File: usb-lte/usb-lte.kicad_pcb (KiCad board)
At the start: 4 copper layers, 26 x 45 mm, 58 parts, among them J1 Sim slot, J2 Conn_Coaxial, J3 Conn_Coaxial, J4 Conn_Coaxial, J5 Conn_01x02_Pin, P1 USB_C_Plug_USB2.0, Q1 BC847W, Q2 BC847W, U1 AP2112K-3.3, U2 EG95

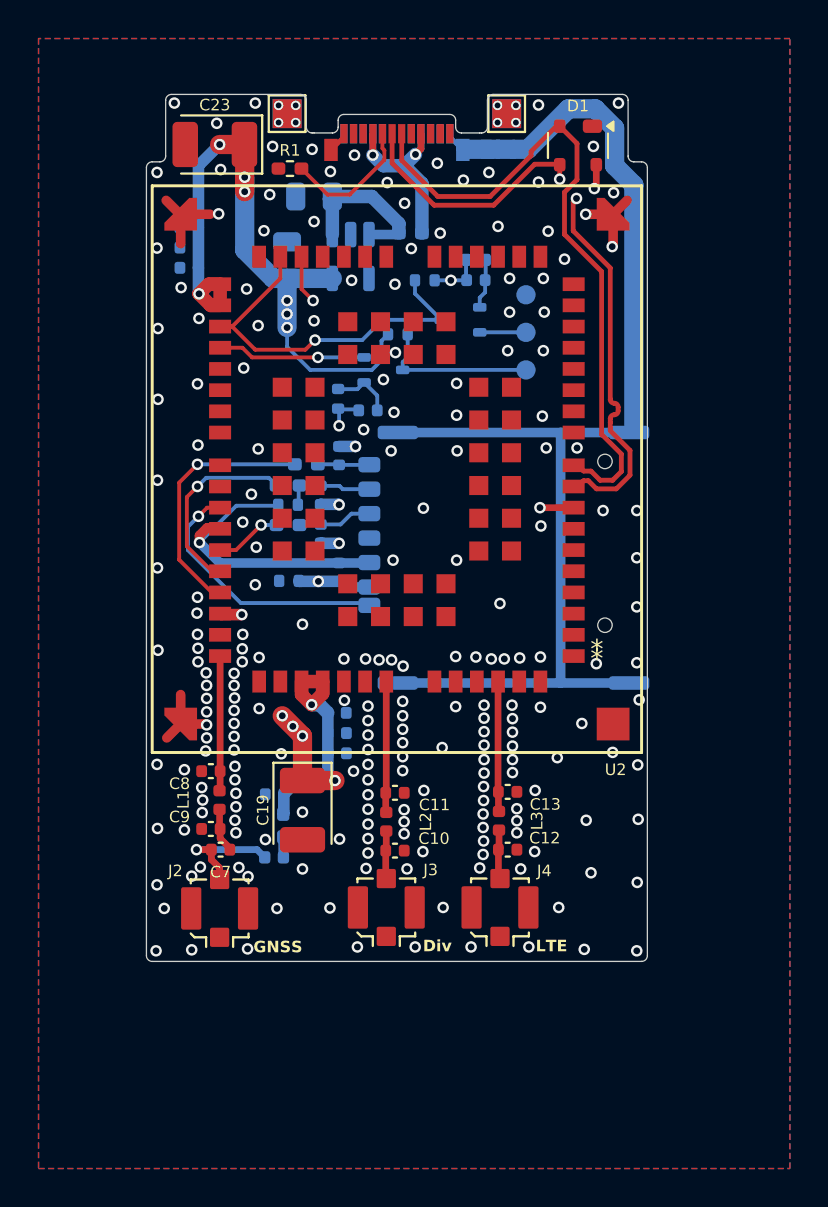
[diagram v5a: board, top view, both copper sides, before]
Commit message: Use SMPS and 3.8V for module
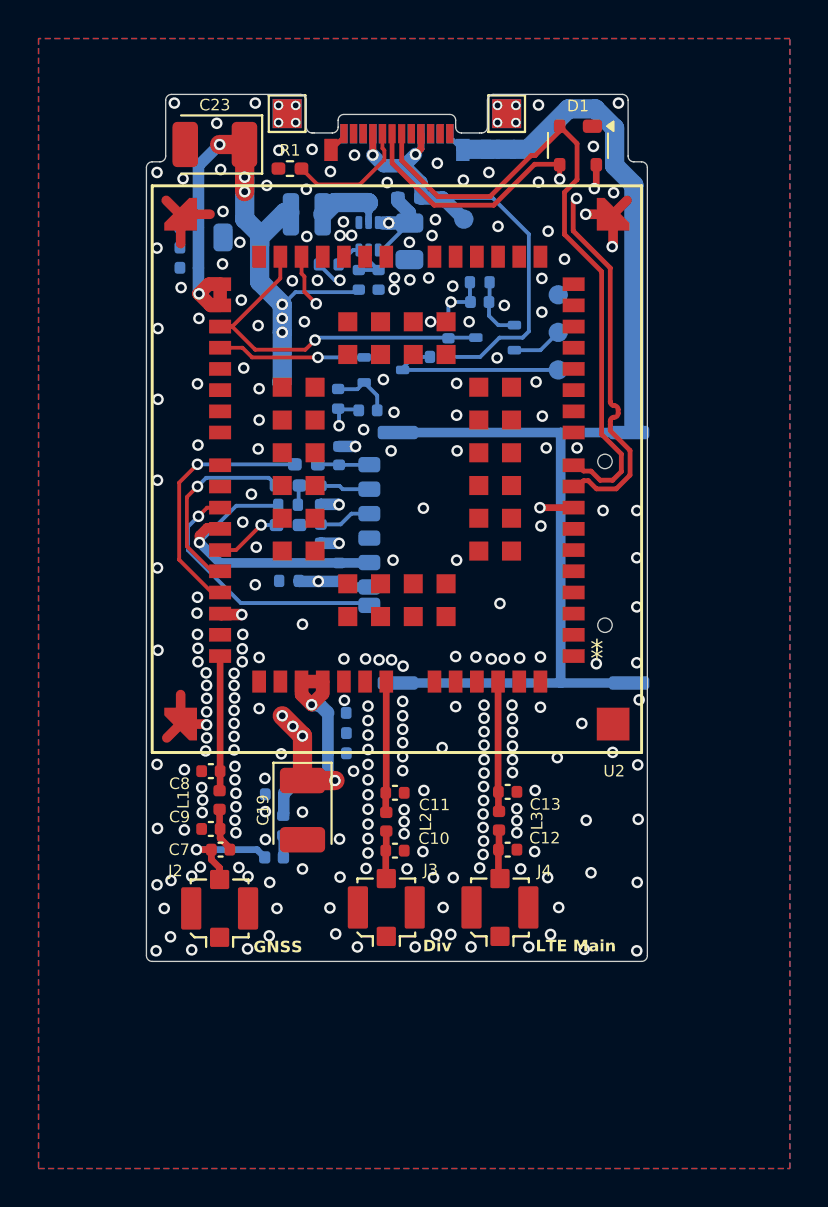
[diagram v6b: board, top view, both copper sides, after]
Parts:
- added L5: 1uH, Inductor_SMD:L_APV_ANR252012, B.Cu at (145.9, 95.1)
- added R13: 510k, Resistor_SMD:R_0402_1005Metric, B.Cu at (148.6, 98.5)
- added R14: 100k, Resistor_SMD:R_0402_1005Metric, B.Cu at (149.7, 98.5)
- added R15: 499k, Resistor_SMD:R_0402_1005Metric, B.Cu at (147.1, 97.7)
- added TP8: TestPoint, footprints:TestPoint_Pad_1mm, B.Cu at (154.1, 95.4)
- added TP9: TestPoint, footprints:TestPoint_Pad_1mm, B.Cu at (144.6, 103.8)
- C1: value 10uF -> 4.7uF
- C2: value 10uF -> 22uF
- R5: footprint Resistor_SMD:R_0402_1005Metric_Pad0.72x0.64mm_HandSolder -> Resistor_SMD:R_0402_1005Metric
- U1: value AP2112K-3.3 -> TPS62A02APDDC; footprint Package_TO_SOT_SMD:SOT-23-5 -> Package_TO_SOT_SMD:SOT-563
- moved C1 5.47 mm to (151.2, 96.5), turned to -90 degrees
- moved R10 2.78 mm to (153.3, 101.0), turned to 90 degrees
- moved C2 2.65 mm to (142.5, 96.3), turned to 0 degrees
- moved R9 2.47 mm to (152.8, 102.5), turned to 180 degrees
- moved Q2 2.02 mm to (155.7, 101.5)
- moved R8 1.83 mm to (151.2, 94.3)
- moved TP5 1.67 mm to (159.0, 103.2)
- moved TP6 1.67 mm to (159.0, 101.2)
- moved TP7 1.67 mm to (159.0, 99.3)
- moved U1 1.40 mm to (149.1, 96.3)
- moved R12 1.18 mm to (154.9, 98.7)
- moved C15 1.15 mm to (154.9, 99.7)
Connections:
- net UART_RX_3V3 renamed UART_RX_5V
- net UART_TX_3V3 renamed UART_TX_5V
- C16 pad 1: +3V3 -> VDD
- C17 pad 1: +3V3 -> VDD
- C18 pad 1: +3V3 -> VDD
- C19 pad 1: +3V3 -> VDD
- C2 pad 1: +3V3 -> GND
- C2 pad 2: GND -> VDD
- C20 pad 1: +3V3 -> VDD
- C21 pad 1: +3V3 -> VDD
- C22 pad 1: +3V3 -> VDD
- C23 pad 1: +3V3 -> VDD
- C24 pad 1: +3V3 -> VDD
- R5 pad 2: +3V3 -> VDD
- R9 pad 1: +3V3 -> VBUS
- U1 pad 1: Net-(U1-EN) -> GND
- U1 pad 2: GND -> Net-(U1-SW)
- U1 pad 4: unconnected-(U1-NC-Pad4) -> Net-(U1-EN)
- U1 pad 5: +3V3 -> Net-(U1-FB)
- U2 pad 32: +3V3 -> VDD
- U2 pad 33: +3V3 -> VDD
- U2 pad 52: +3V3 -> VDD
- U2 pad 53: +3V3 -> VDD
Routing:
- net +3V3: track 76.3 -> 0.00 mm, vias 12 -> 0
- net VDD: track 0.00 -> 73.9 mm, vias 0 -> 12
- net VBUS: track 43.0 -> 58.8 mm
- net Net-(U1-SW): track 0.00 -> 3.66 mm
- net Net-(U1-FB): track 0.00 -> 3.00 mm
- net Net-(U1-EN): track 8.09 -> 10.6 mm, vias 0 -> 2
- net UART_TX_5V: track 8.36 -> 9.83 mm
- net Net-(U1-PG): track 0.00 -> 1.36 mm
- net UART_RX_1V8: track 20.5 -> 19.3 mm
- net Net-(Q2-B): track 2.38 -> 3.28 mm
- net GND: vias 223 -> 250
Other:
- board text added: "3.8V"
- board text added: "5V"
- board text added: "LTE Main"
- board text added: "UART 5V"
- board text removed: "LTE"
- board text removed: "UART 3.3V"

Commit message: Make USB C 2.0 reversible
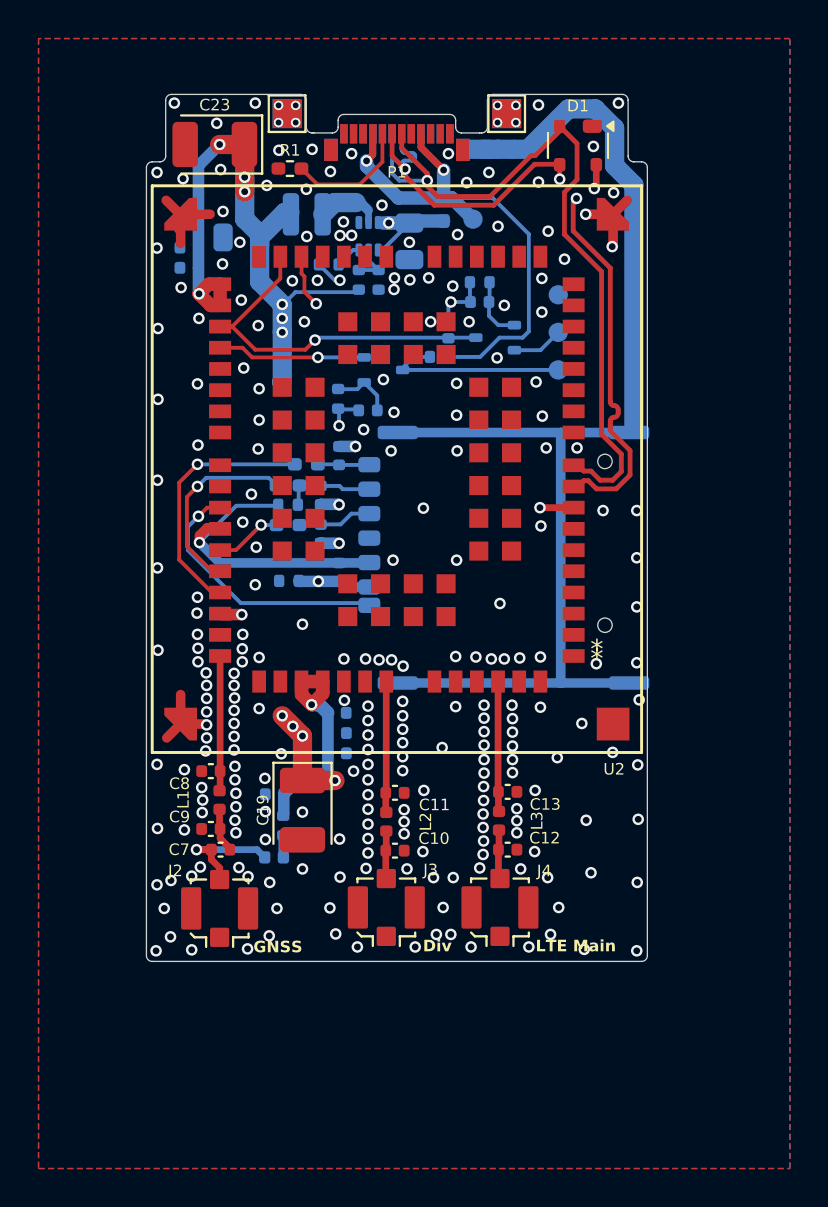
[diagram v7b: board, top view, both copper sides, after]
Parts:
- P1: footprint Expansion_Card:USB_C_Plug_Molex_105444 -> footprints:USB_C_Plug_Molex_105444
- R16: renamed from J5; value Conn_01x02_Pin -> 0R
- moved R8 1.87 mm to (153.0, 94.9), turned to -90 degrees
- moved TP8 0.48 mm to (154.6, 95.4)
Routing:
- net USB_DN: track 34.6 -> 38.6 mm, vias 0 -> 1
- net VBUS: track 58.8 -> 62.4 mm
- net USB_DP: track 33.5 -> 36.5 mm, vias 2 -> 3
- net GND: track 15.5 -> 13.2 mm, vias 250 -> 249

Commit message: Minor changes
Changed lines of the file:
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@@
 		(tags "resistor")
 		(property "Reference" "R12"
-			(at 0 1.8 0)
+			(at 1.8 0 0)
 			(layer "B.SilkS")
 			(effects
@@
 		(tags "capacitor")
 		(property "Reference" "C15"
-			(at 0 1.95 0)
+			(at 1.8 0 0)
 			(layer "B.SilkS")
 			(effects
@@
 		(tags "capacitor")
 		(property "Reference" "C1"
-			(at 0.25 -1.45 90)
+			(at -2.3 0 90)
 			(layer "B.SilkS")
 			(effects
@@
 		(tags "resistor handsolder")
 		(property "Reference" "R8"
-			(at -0.65 0.925 90)
+			(at 1.675 0 90)
 			(layer "B.SilkS")
 			(effects
@@
 	)
 	(gr_text "5V"
-		(at 156.45 95.75 0)
+		(at 155.15 96.9 0)
 		(layer "B.SilkS")
 		(effects
@@
 	)
 	(via
-		(at 152.25 98.425)
+		(at 152 98.55)
 		(size 0.6)
 		(drill 0.35)
